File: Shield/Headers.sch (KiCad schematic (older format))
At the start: 21 parts, among them J1 EXPANSION, J10 E0 COOL, J11 E0 TEMP, J12 E1 H&T, J13 FAN_0, J14 E0 MOT/STOP, J15 E0 MOT/STOP, J19 E0 HEAT, J2 PWR, J23 POWER IN, J24 PWR, J28 Probe, J4 PWR, J5 E2 H&T, J6 EXPANSION2, J7 MOTORS, J8 E2 MOT/STOP, J9 E1 MOT/STOP, K1 E0 FAN, P1 STEP, P2 E0 H&T

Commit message: Split shield development into two stages:
Stage 1: 2 heaters + 2 stepper drivers
Stage 2: 2 extra stepper drivers, 5-motor stepper ribbon, expansion connector

This is the cut down version ready for Stage 1.
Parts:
- removed J6: EXPANSION2, symbol CONN2X15
- removed J7: MOTORS, symbol CONN2X18
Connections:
- net labels removed: E3_MOT_1A, E3_MOT_1B, E3_MOT_2A, E3_MOT_2B, E3_STOP_CONN, E4_MOT_1A, E4_MOT_1B, E4_MOT_2A, E4_MOT_2B, E4_STOP_CONN
- wire segments 347 -> 279
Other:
- note removed: "5 Motor\nribbon\nheader"

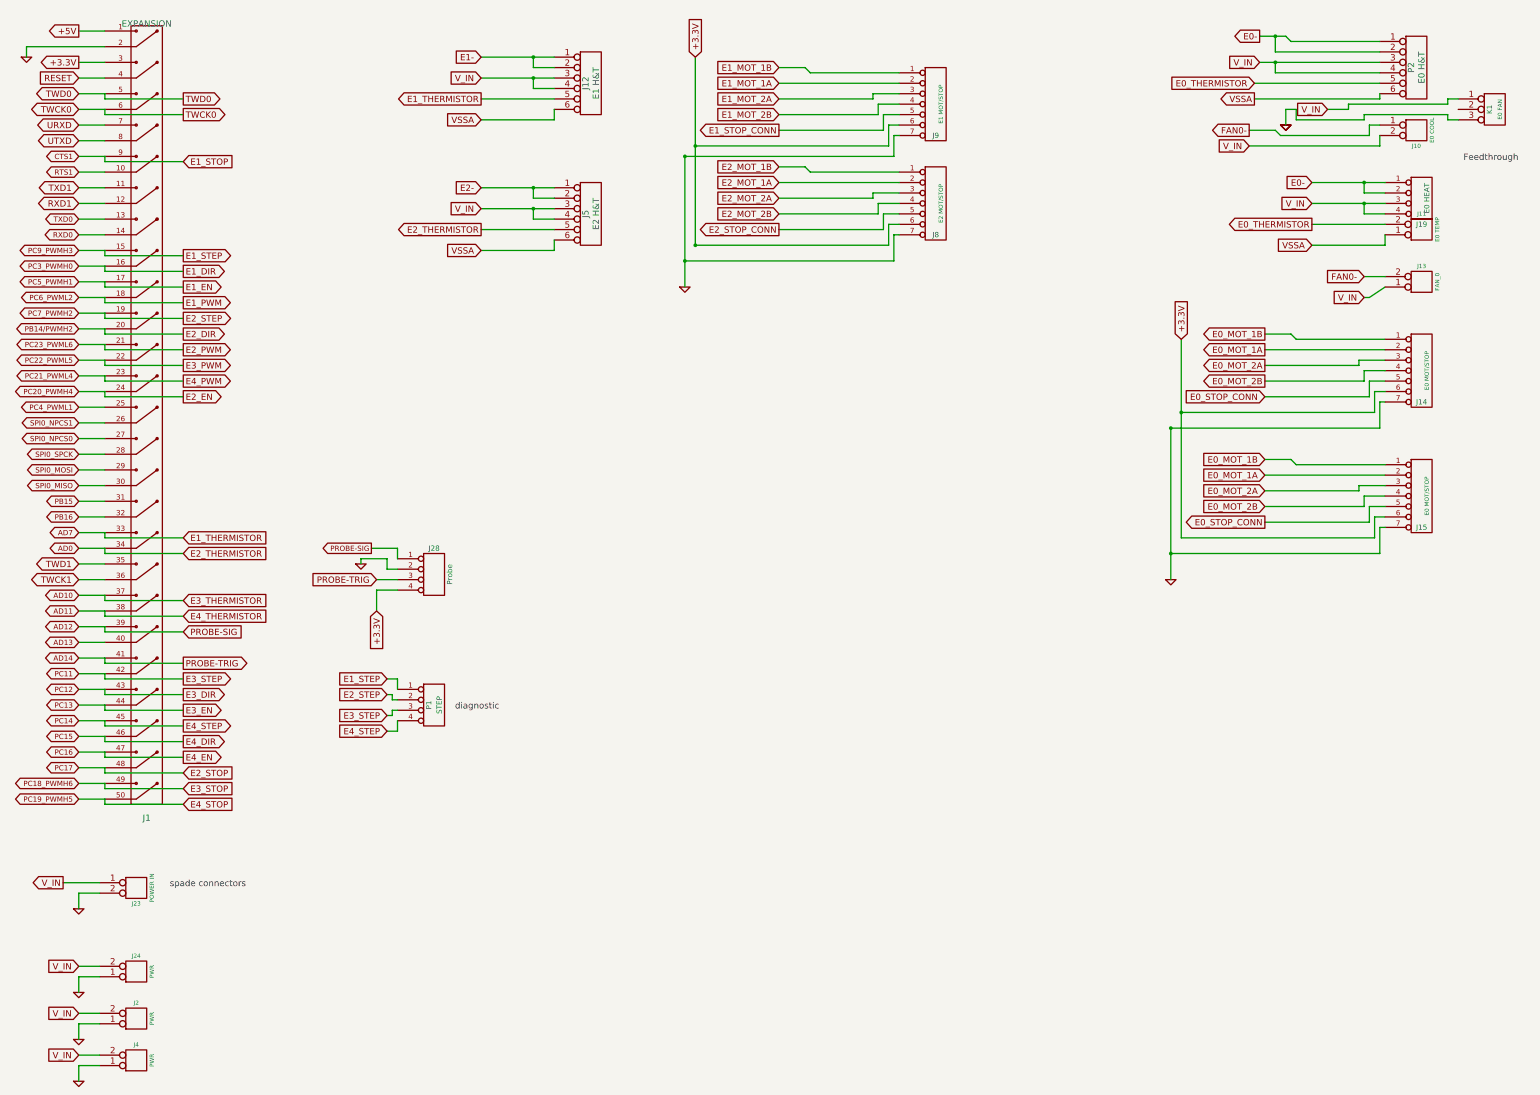
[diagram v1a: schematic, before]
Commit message: Shield spade connectirs used for power.
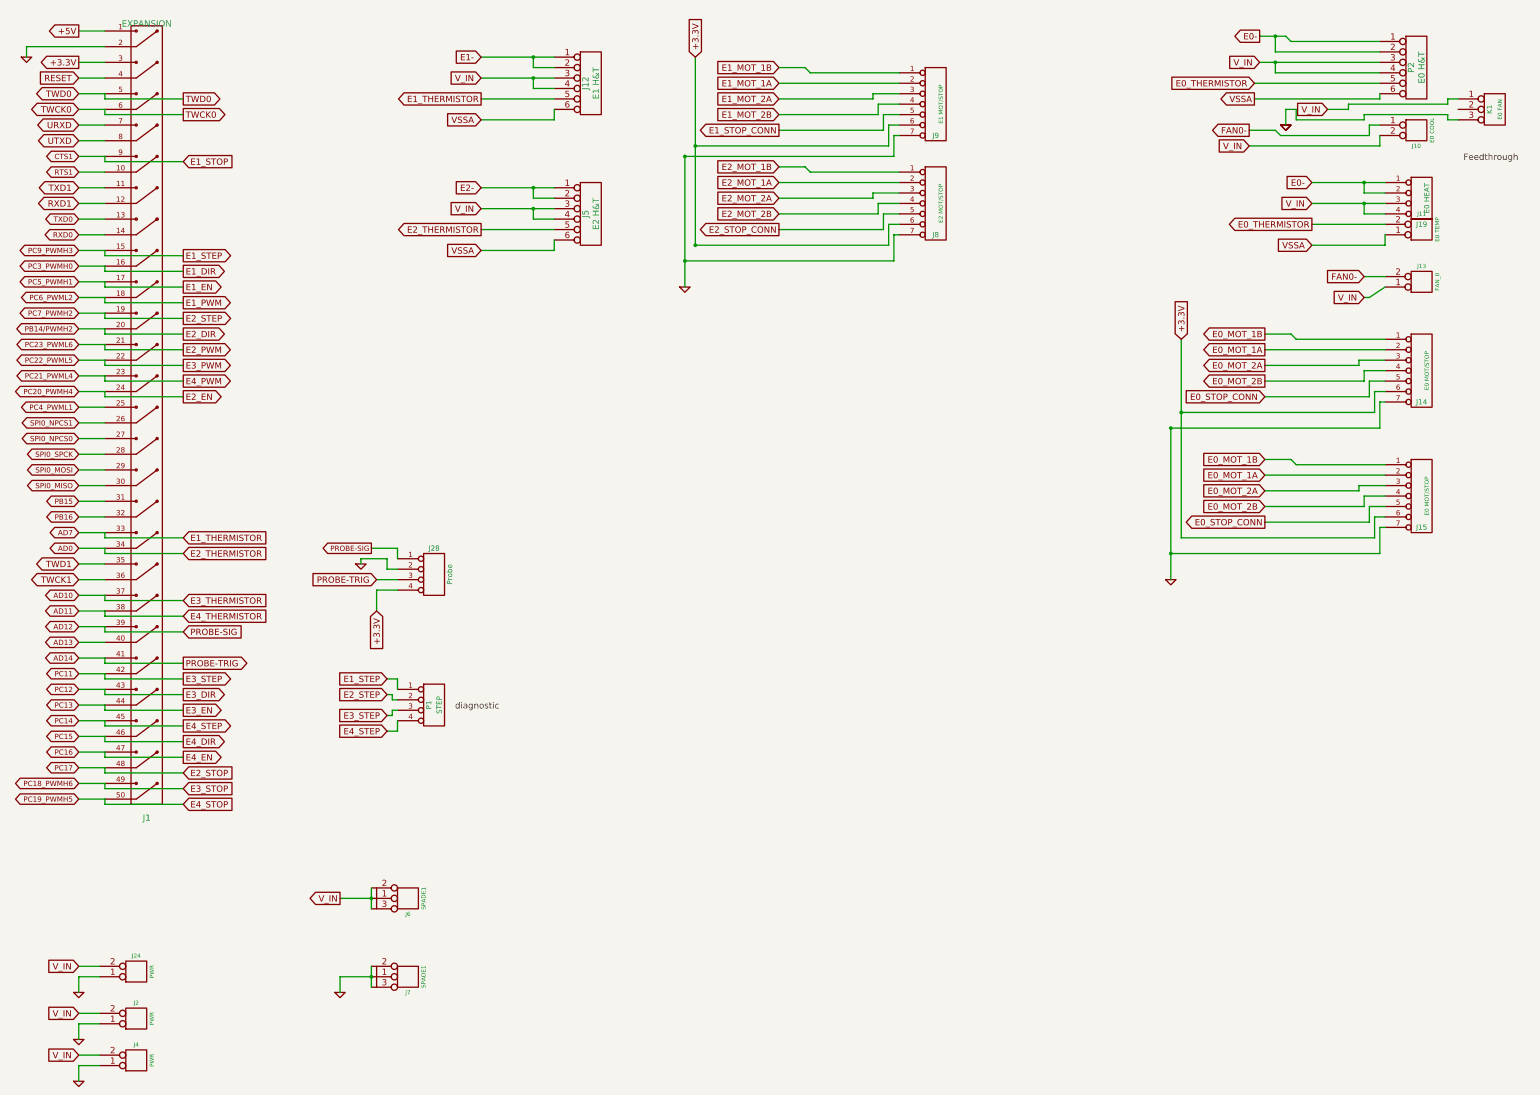
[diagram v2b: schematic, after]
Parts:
- removed J23: POWER IN, symbol CONN2
- added J6, J7: SPADE1, symbol SPADE1
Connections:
- net GND: now also J7.1 (P1), J7.2, J7.3
- net V_IN: now also J6.1 (P1), J6.2, J6.3
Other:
- note removed: "spade connectors"
